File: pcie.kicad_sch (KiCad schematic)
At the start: 2 parts, among them U1 MIMX8MM6DVTLZAA

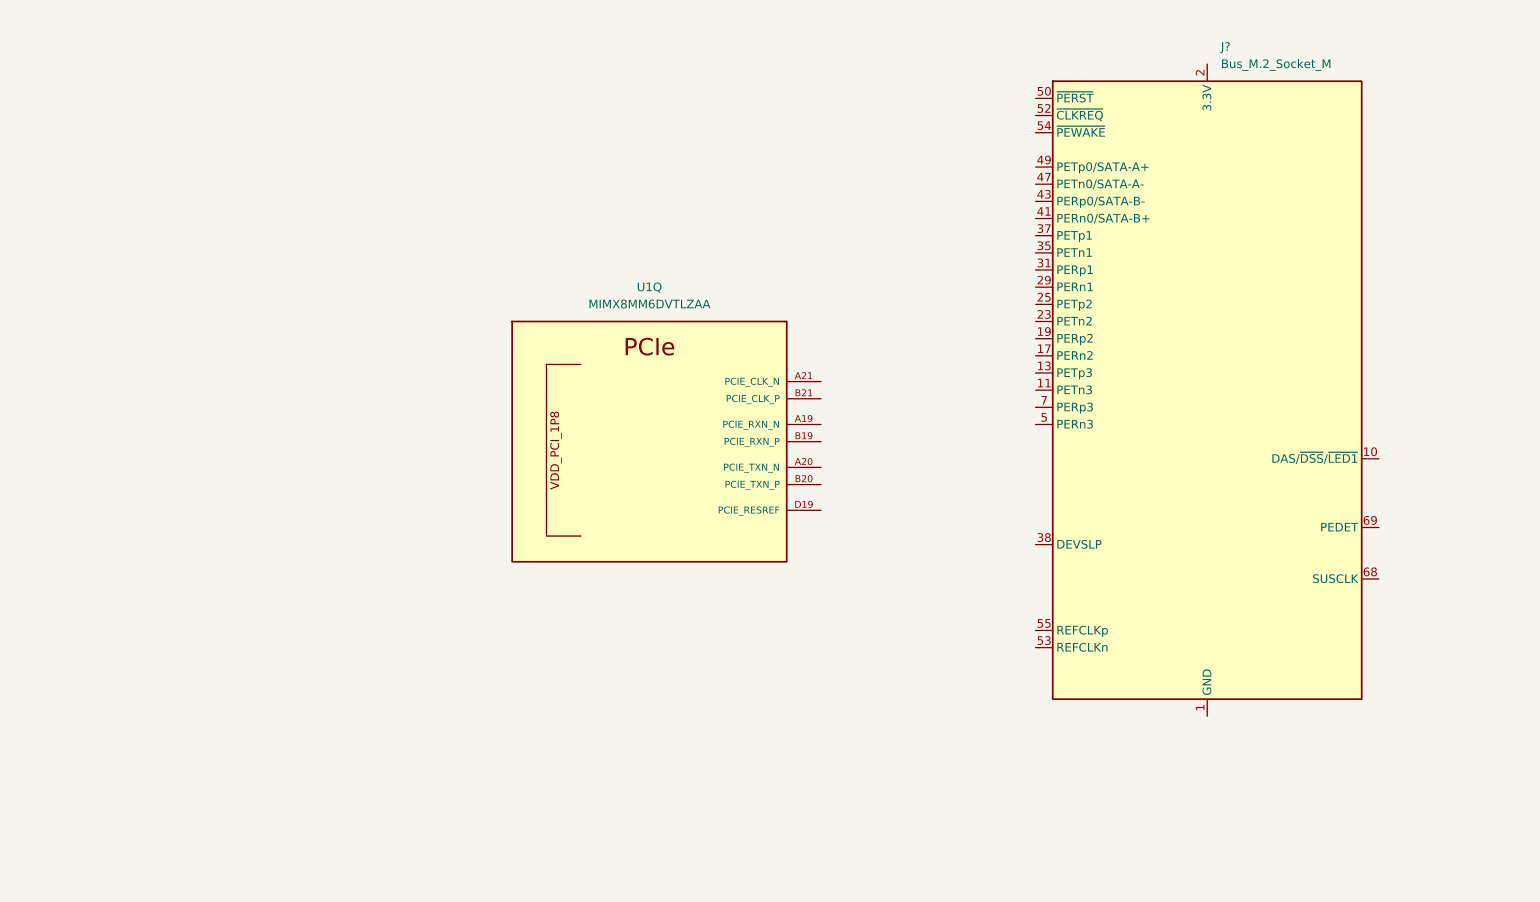
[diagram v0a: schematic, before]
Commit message: enet sch done, other misc sch work
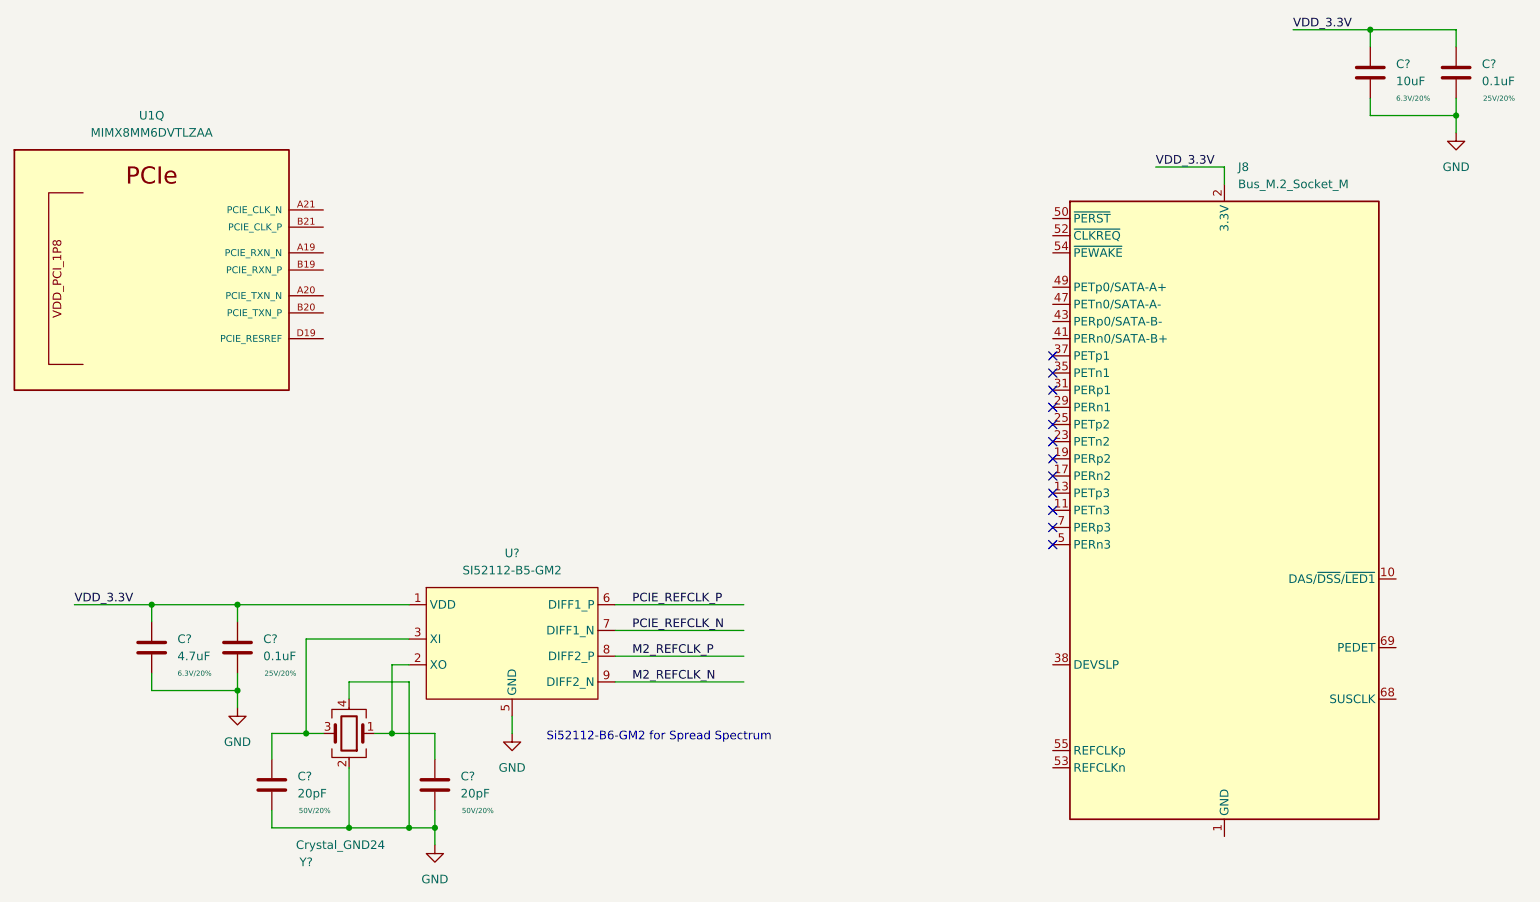
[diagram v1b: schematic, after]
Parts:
- added C?: 10uF, Capacitor_SMD:C_0603_1608Metric, symbol Device:C
- added C? (x2): 0.1uF, Capacitor_SMD:C_0402_1005Metric, symbol Device:C
- added C? (x2): 20pF, Capacitor_SMD:C_0402_1005Metric, symbol Device:C
- added C?: 4.7uF, Capacitor_SMD:C_0402_1005Metric, symbol Device:C
- added U?: SI52112-B5-GM2, Package_DFN_QFN:DFN-10-1EP_3x3mm_P0.5mm_EP1.55x2.48mm, symbol qsbc:SI52112-B5-GM2
- added Y?: Crystal_GND24, symbol Device:Crystal_GND24
- J8: renamed from J?; footprint (none) -> qsbc:1-2199230-6
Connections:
- net VDD: now reaches J8.12 (3.3V), J8.14 (3.3V), J8.16 (3.3V), J8.18 (3.3V), J8.2 (3.3V), J8.4 (3.3V), J8.70 (3.3V), J8.72 (3.3V), J8.74 (3.3V)
- net VDD: now also C?.1, C?.1, C?.1, C?.1, U?.1 (VDD), U?.10 (VDD)
- new net: C?.1, U?.2 (XO), Y?.1
- new net: C?.1, U?.3 (XI), Y?.3
- new net GND: C?.2, C?.2, C?.2, C?.2, C?.2, C?.2, U?.4 (GND), U?.5 (GND), Y?.2, Y?.4
- new net M2_REFCLK_N: U?.9 (DIFF2_N)
- new net M2_REFCLK_P: U?.8 (DIFF2_P)
- new net PCIE_REFCLK_N: U?.7 (DIFF1_N)
- new net PCIE_REFCLK_P: U?.6 (DIFF1_P)
- no-connect marks 0 -> 12
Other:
- note added: "Si52112-B6-GM2 for Spread Spectrum"
- moved on the sheet: J8, U1Q

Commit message: pcie done, misc fixes for usb, enet
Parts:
- added C120, C121: 0.22uF, Capacitor_SMD:C_0402_1005Metric, symbol Device:C
- added C124, C125: 10uF, Capacitor_SMD:C_0603_1608Metric, symbol Device:C
- added C126, C127, C? (x2): 0.1uF, Capacitor_SMD:C_0402_1005Metric, symbol Device:C
- added D?: LED_YELLOW, LED_SMD:LED_0603_1608Metric, symbol Device:LED
- added R65: 8,2K, Resistor_SMD:R_0402_1005Metric, symbol Device:R
- added R66, R67, R68, R69, R? (x2): 10K, Resistor_SMD:R_0402_1005Metric, symbol Device:R
- added R?: 2.2K, Resistor_SMD:R_0402_1005Metric, symbol Device:R
- added U24, U25: 74LVC1G07, Package_TO_SOT_SMD:SOT-553, symbol 74xGxx:74LVC1G07
- Y3: renamed from Y?; value Crystal_GND24 -> 25MHz
- gave numbers to parts that had none: 7
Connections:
- net GND: now also J8.1 (GND), J8.15 (GND), J8.21 (GND), J8.27 (GND), J8.3 (GND), J8.33 (GND), J8.39 (GND), J8.45 (GND), J8.51 (GND), J8.57 (GND), J8.71 (GND), J8.73 (GND), J8.75 (GND), J8.9 (GND), C124.2, C125.2, C126.2, C127.2, C?.2, C?.2, R65.2, U24.3 (GND), U25.3 (GND)
- net M2_REFCLK_N: now also J8.53 (REFCLKn)
- net M2_REFCLK_P: now also J8.55 (REFCLKp)
- net PCIE_REFCLK_N: now also U1.B21 (PCIE_CLK_P)
- net PCIE_REFCLK_P: now also U1.A21 (PCIE_CLK_N)
- net VDD: now also C124.1, C125.1, C126.1, C127.1, R66.1, R67.1, R68.1, R69.1, R?.1
- net PCIE_RX_N: now reaches U1.A19 (PCIE_RXN_N)
- net PCIE_RX_N: now also J8.41 (PERn0/SATA-B+)
- net PCIE_TX_N: now reaches U1.A20 (PCIE_TXN_N)
- net PCIE_TX_N: now also C120.1
- net PCIE_RX_P: now reaches U1.B19 (PCIE_RXN_P)
- net PCIE_RX_P: now also J8.43 (PERp0/SATA-B-)
- net PCIE_TX_P: now reaches U1.B20 (PCIE_TXN_P)
- net PCIE_TX_P: now also C121.1
- net PCIE_RESREF: now reaches U1.D19 (PCIE_RESREF)
- net PCIE_RESREF: now also R65.1
- net at J8.10 (DAS/~{DSS}/~{LED1}): now also D?.1 (K)
- net PCIE_TX_R_P: now reaches J8.47 (PETn0/SATA-A-)
- net PCIE_TX_R_P: now also C121.2
- net PCIE_TX_R_N: now reaches J8.49 (PETp0/SATA-A+)
- net PCIE_TX_R_N: now also C120.2
- net ~{M2_RESET_3.3V}: now reaches J8.50 (~{PERST})
- net ~{M2_RESET_3.3V}: now also R68.2, U24.4
- net ~{M2_CLKREQ_3.3V}: now reaches J8.52 (~{CLKREQ})
- net ~{M2_CLKREQ_3.3V}: now also R67.2
- net ~{M2_WAKE_3.3V}: now reaches J8.54 (~{PEWAKE})
- net ~{M2_WAKE_3.3V}: now also R66.2, U25.2
- net at J8.69 (PEDET): now also R69.2
- new net: D?.2 (A), R?.2
- new net VCC: C?.1, C?.1, R?.1, R?.1, U24.5 (VCC), U25.5 (VCC)
- new net ~{M2_RESET}: R?.2, U24.2
- new net ~{M2_WAKE}: R?.2, U25.4
- no-connect marks 12 -> 14
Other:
- moved on the sheet: C122, C123

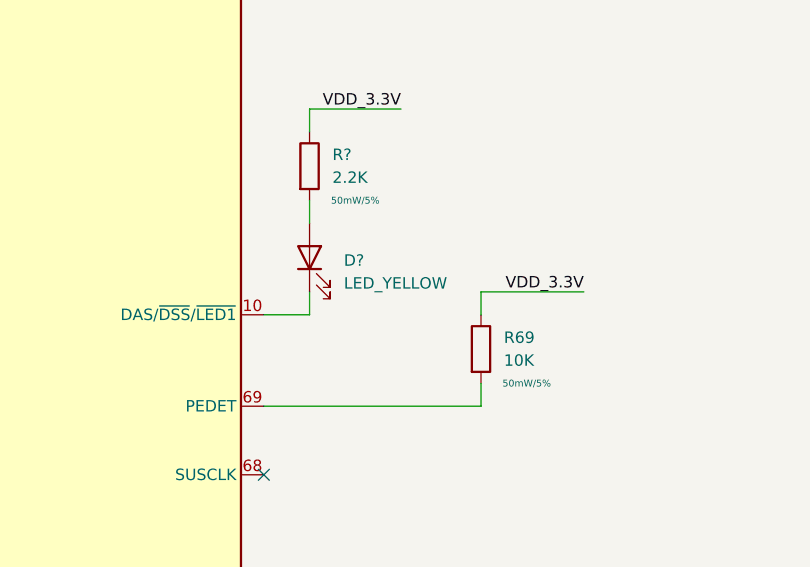
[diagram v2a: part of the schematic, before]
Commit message: storage done, peri work, misc fixes
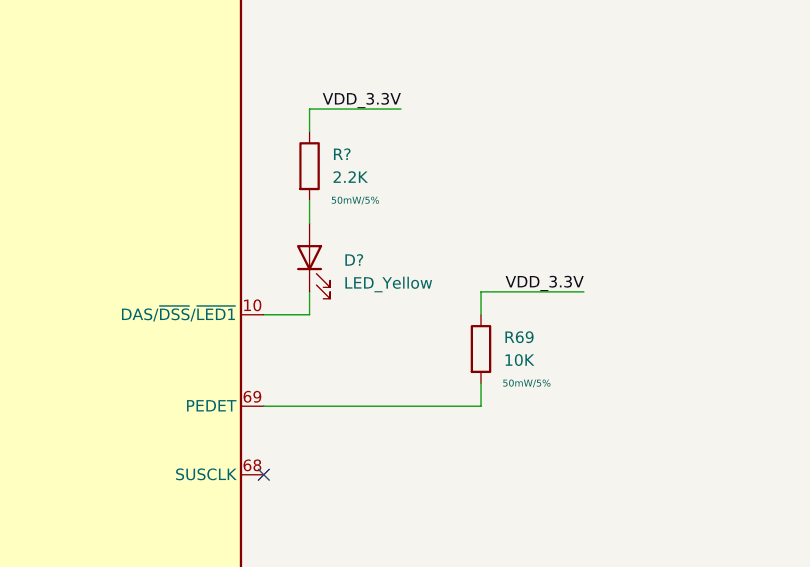
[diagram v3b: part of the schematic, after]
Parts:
- D?: value LED_YELLOW -> LED_Yellow
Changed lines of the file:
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@@
       (effects (font (size 1.27 1.27)) (justify right))
     )
-    (property "Value" "LED_YELLOW" (id 1) (at 270.51 110.8074 90)
+    (property "Value" "LED_Yellow" (id 1) (at 270.51 110.8074 90)
       (effects (font (size 1.27 1.27)) (justify right))
     )
